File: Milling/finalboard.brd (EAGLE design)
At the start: 82.5 x 73.3 mm, 23 parts, among them IC1 317EMP, X1 332-02, X10 332-02, X11 332-02, X2 332-02, X3 332-02, X4 332-02, X5 332-02, X6 332-02, X7 332-02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

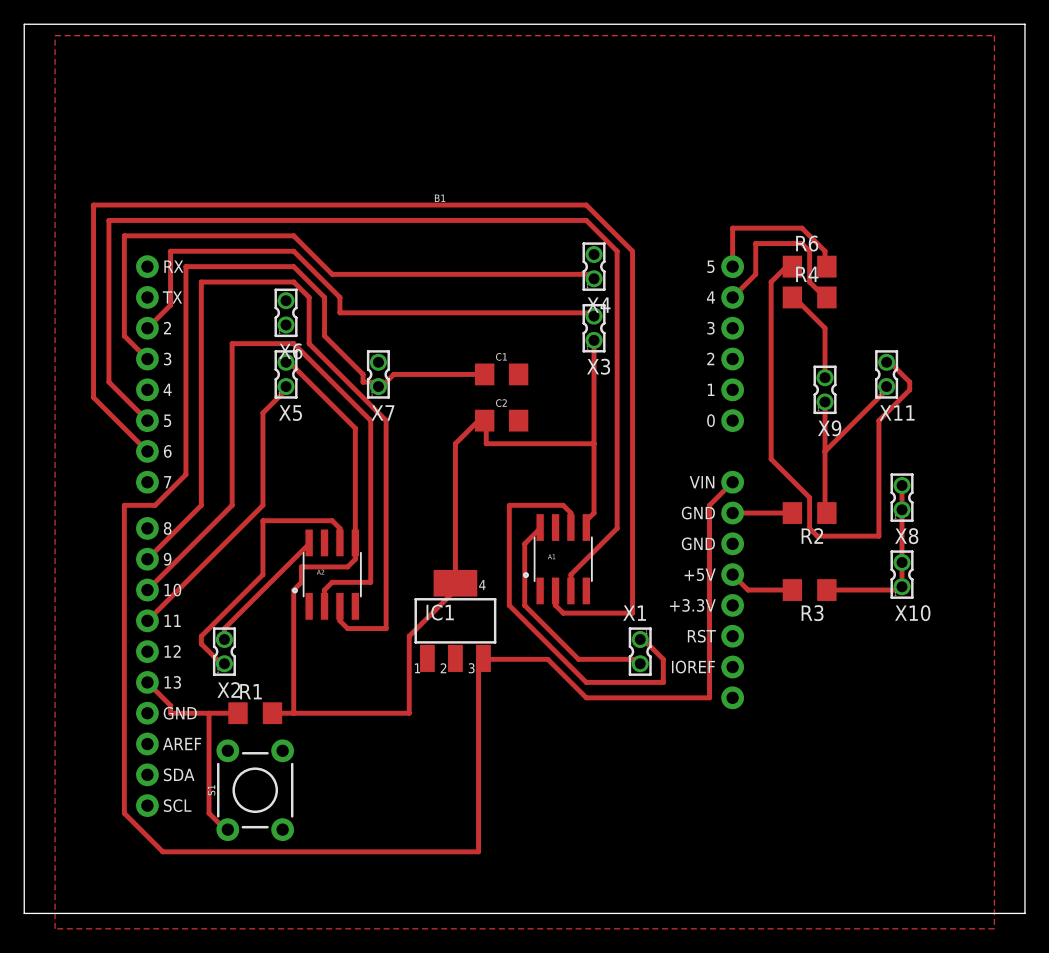
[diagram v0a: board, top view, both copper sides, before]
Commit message: fixed eagle files
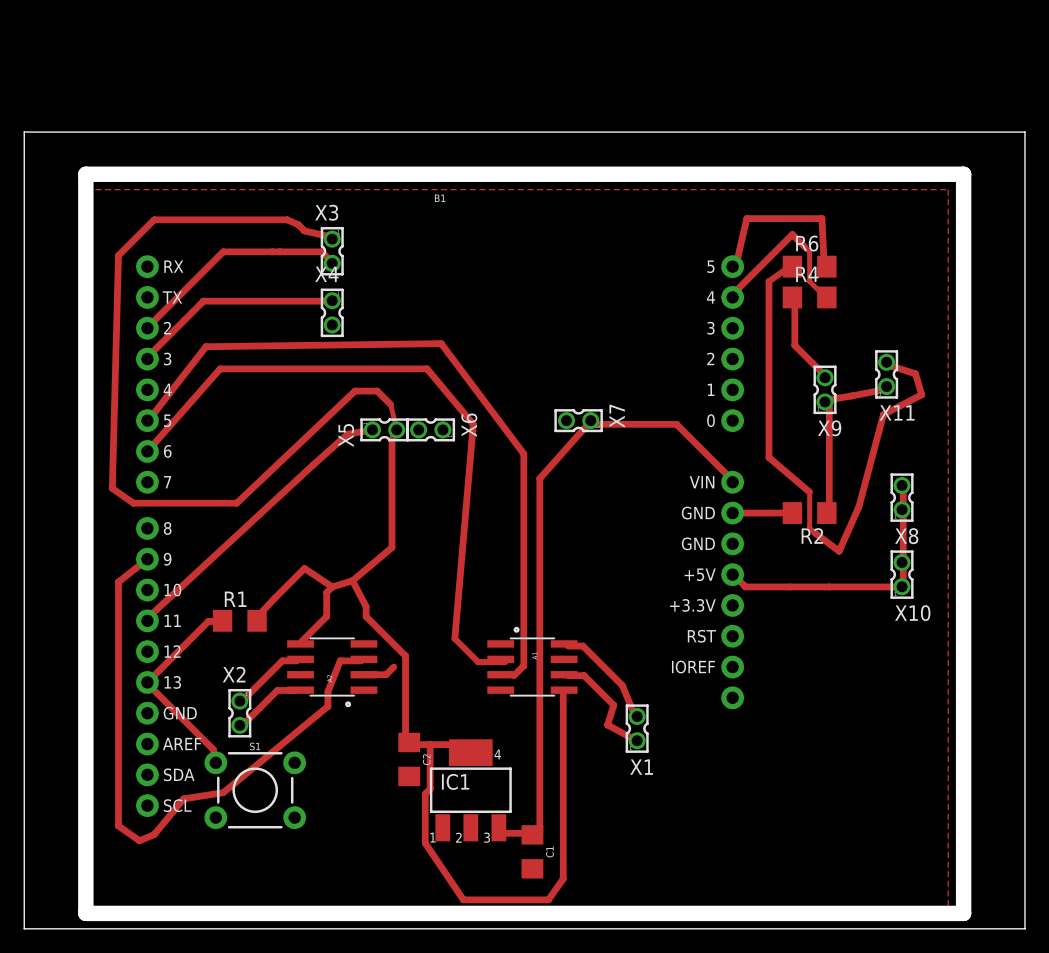
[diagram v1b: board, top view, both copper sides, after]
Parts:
- removed R3: (no value), eagle-ltspice:R1206
- moved C1 39.5 mm to (-33.0, 22.9), turned to 270 degrees
- moved C2 29.0 mm to (-43.2, 30.5), turned to 270 degrees
- moved X3 22.5 mm to (-49.5, 72.4), turned to 180 degrees
- moved X4 21.9 mm to (-49.5, 67.3), turned to 180 degrees
- moved X7 16.9 mm to (-29.2, 58.4), turned to 90 degrees
- moved X6 15.4 mm to (-41.4, 57.7), turned to 90 degrees
- moved IC1 14.0 mm to (-38.1, 27.9)
- moved X5 9.33 mm to (-45.2, 57.7), turned to 270 degrees
- moved A1 9.25 mm to (-33.0, 38.1), turned to 270 degrees
- moved R1 7.73 mm to (-57.1, 41.9)
- moved A2 7.62 mm to (-49.5, 38.1), turned to 90 degrees
- moved X1 6.36 mm to (-24.4, 33.0), turned to 0 degrees
- moved X2 5.24 mm to (-57.1, 34.3), turned to 180 degrees
- turned S1 to 0 degrees
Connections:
- removed net N$14: R3.1, X10.1, X10.2, X8.1, X8.2
- net N$18: now also X10.1, X10.2, X8.1, X8.2; no longer R3.2
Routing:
- net VCC: track 166.0 -> 53.2 mm
- net +5V: track 101.1 -> 157.7 mm
- net N$4: track 56.0 -> 2.73 mm
- net N$2: track 105.8 -> 55.2 mm
- net N$9: track 51.4 -> 17.3 mm
- net N$1: track 90.4 -> 58.3 mm
- net N$21: track 45.2 -> 18.3 mm
- net N$5: track 35.0 -> 9.58 mm
- net N$3: track 69.3 -> 50.8 mm
- net N$18: track 5.45 -> 22.9 mm
- net N$7: track 23.0 -> 6.39 mm
- net N$14: track 14.8 -> 0.00 mm
- net N$6: track 18.7 -> 9.07 mm
- net N$8: track 10.9 -> 6.19 mm
- net N$19: track 13.0 -> 15.3 mm
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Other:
- board size 82.5 x 73.3 mm -> 82.5 x 65.7 mm
